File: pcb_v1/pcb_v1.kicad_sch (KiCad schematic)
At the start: 14 parts, among them IC1 ESP32-C3-WROOM-02-N4, IC2 DWM3000TR13, IC3 TC1017-3.3VLTTR, J1 Conn_01x04_Pin, J2 1769, J3 Conn_01x04_Pin

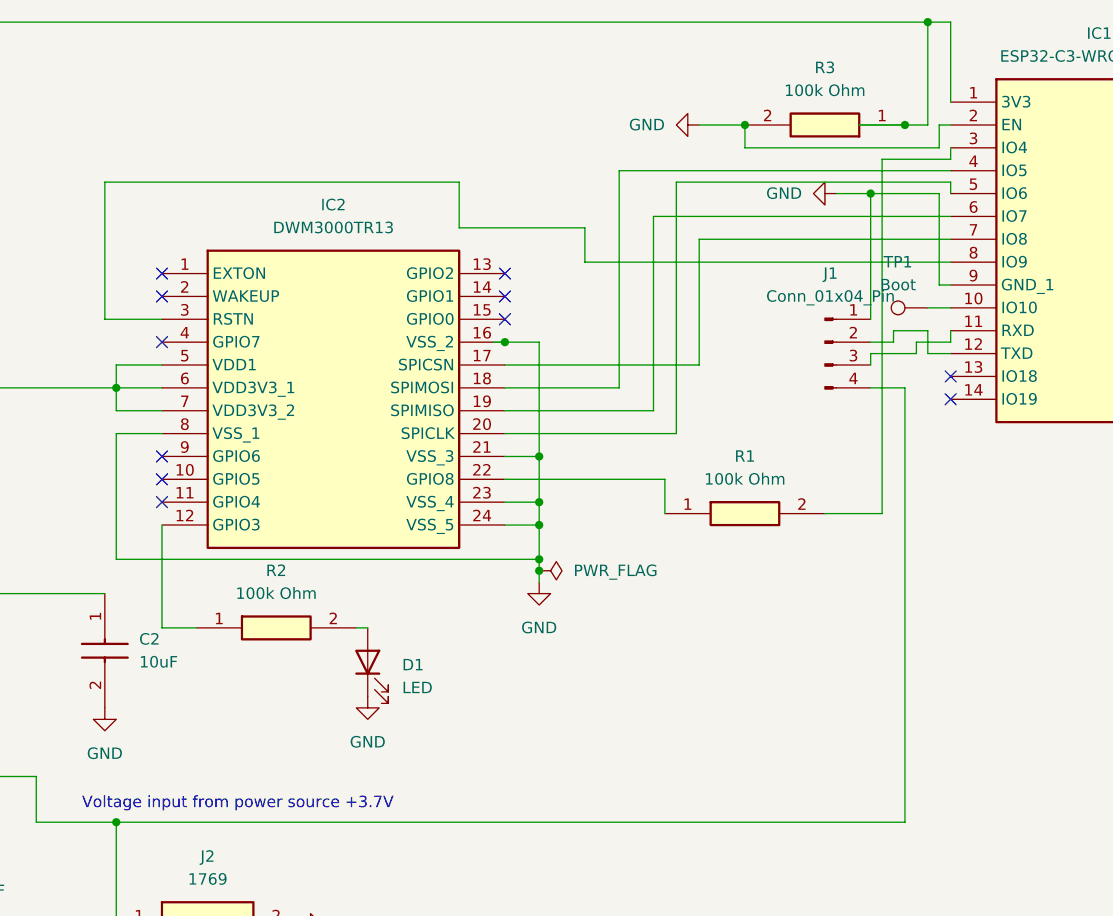
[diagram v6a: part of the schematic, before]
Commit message: small changes to pcb, removed resistors and edited spi pins that connect mcu to uwb
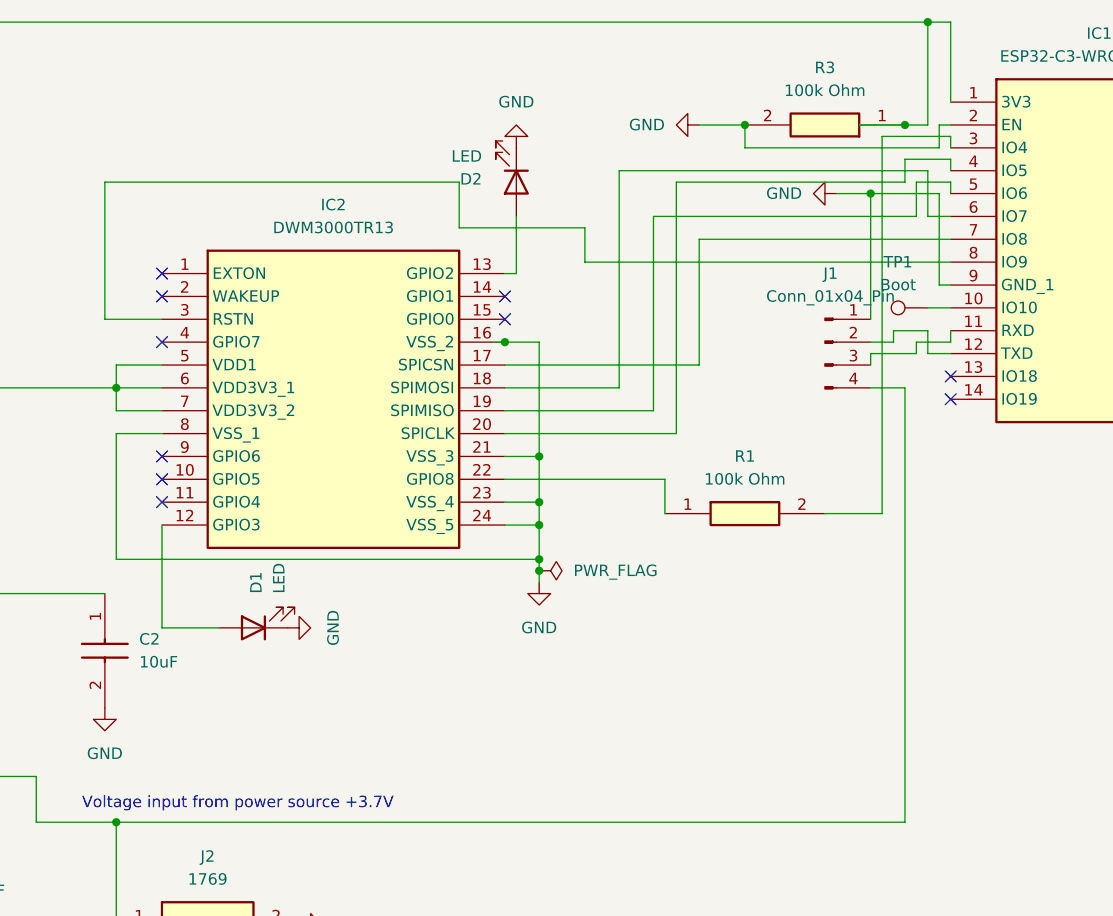
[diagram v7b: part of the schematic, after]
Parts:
- removed R2: 100k Ohm, 100kOhm_footprint:RESC5025X65N, symbol CRGP2010F100K:CRGP2010F100K
- added D2: LED, led_footprint:QED123A4R0, symbol Device:LED
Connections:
- net GND: now also D2.1 (K)
- net at IC2.12 (GPIO3): now also D1.2 (A)
- net at IC2.13 (GPIO2): now also D2.2 (A)
- net at IC2.18 (SPIMOSI): now also IC1.6 (IO7); no longer IC1.4 (IO5)
- net at IC2.19 (SPIMISO): now also IC1.5 (IO6); no longer IC1.6 (IO7)
- net at IC2.20 (SPICLK): now also IC1.4 (IO5); no longer IC1.5 (IO6)
- no-connect marks 11 -> 10
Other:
- moved on the sheet: D1
